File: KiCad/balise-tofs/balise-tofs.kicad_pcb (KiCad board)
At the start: 4 copper layers, 95.4 x 95.4 mm, 97 parts, among them J1 Vin, J10 Conn_02x05_Odd_Even, J11 Conn_02x05_Odd_Even, J12 Conn_02x05_Odd_Even, J13 Conn_02x05_Odd_Even, J14 Conn_02x05_Odd_Even, J15 Conn_02x05_Odd_Even, J16 Conn_02x05_Odd_Even, J17 Conn_02x05_Odd_Even, J18 Conn_02x05_Odd_Even, J19 Conn_02x05_Odd_Even, J2 Conn_01x03, J20 Conn_02x05_Odd_Even, J21 Conn_02x05_Odd_Even, Q1 Q_PMOS_GDS, U1 AP63203WU-7, U2 NUCLEO-G431KB, U3 PCA9535CPW, U4 AP63205WU-7, U5 74AHCT1G125

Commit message: ajout des plans
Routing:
- added copper zone on In2.Cu, net 3V3_SENS
- added copper zone on In1.Cu, net GND
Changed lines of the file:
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@@
 		(layer "Edge.Cuts")
+	)
+	(zone
+		(net 1)
+		(net_name "GND")
+		(layer "In1.Cu")
+		(hatch edge 0.5)
+		(connect_pads
+			(clearance 0.5)
+		)
+		(min_thickness 0.25)
+		(filled_areas_thickness no)
+		(fill yes
+			(thermal_gap 0.5)
+			(thermal_bridge_width 0.5)
+		)
+		(polygon
+			(pts
+				(xy 100.584 100.584) (xy 200.406 100.076) (xy 200.406 198.882) (xy 100.838 199.898)
+			)
+		)
+	)
+	(zone
+		(net 5)
+		(net_name "3V3_SENS")
+		(layer "In2.Cu")
+		(hatch edge 0.5)
+		(priority 1)
+		(connect_pads
+			(clearance 0.5)
+		)
+		(min_thickness 0.25)
+		(filled_areas_thickness no)
+		(fill yes
+			(thermal_gap 0.5)
+			(thermal_bridge_width 0.5)
+		)
+		(polygon
+			(pts
+				(xy 100.838 100.076) (xy 200.66 100.076) (xy 200.152 198.374) (xy 101.092 199.898)
+			)
+		)
 	)
 	(embedded_fonts no)

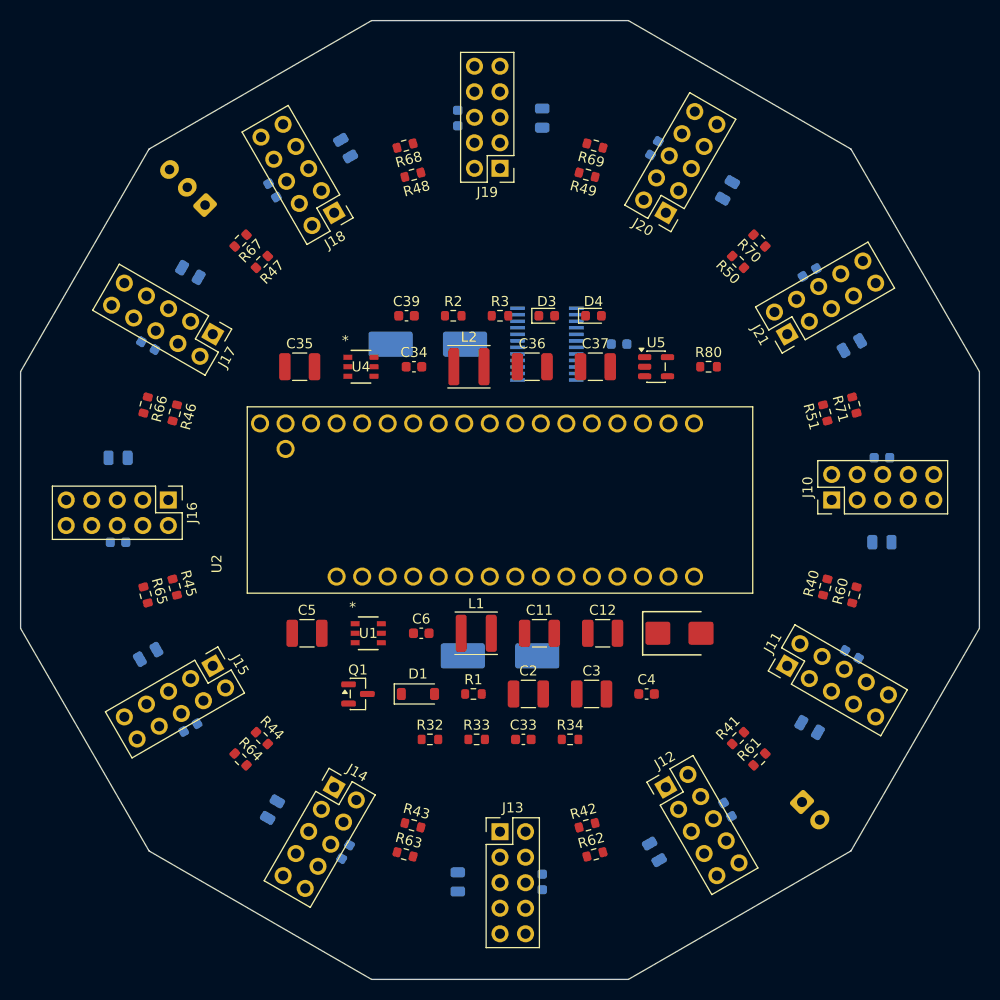
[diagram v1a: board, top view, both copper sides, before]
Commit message: passage à kicad 10 et début du routage
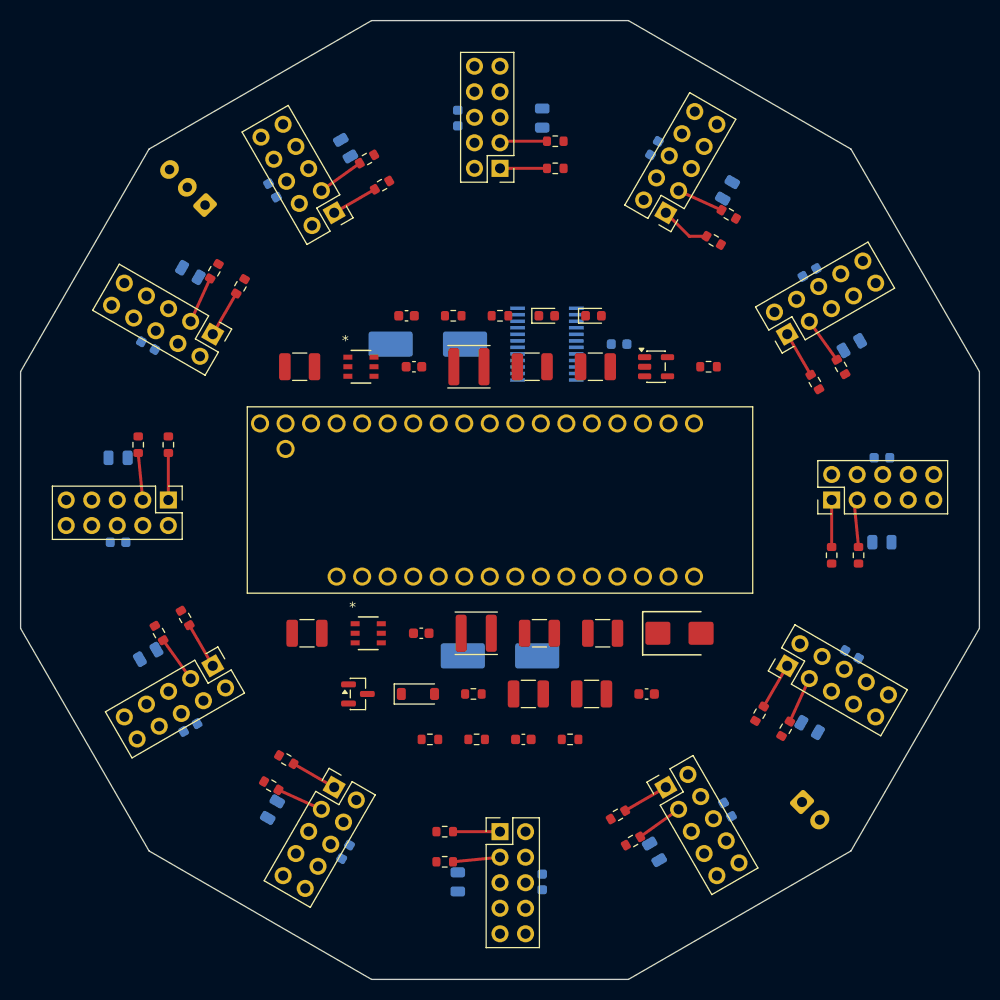
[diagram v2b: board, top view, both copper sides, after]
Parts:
- moved R45 4.83 mm to (116.1, 163.2), turned to -60 degrees
- moved R48 4.83 mm to (136.8, 116.1), turned to -150 degrees
- moved R42 4.83 mm to (163.2, 183.9), turned to 30 degrees
- moved R51 4.83 mm to (183.9, 136.8), turned to 120 degrees
- moved R44 4.83 mm to (127.2, 178.4), turned to -30 degrees
- moved R47 4.83 mm to (121.6, 127.2), turned to -120 degrees
- moved R41 4.83 mm to (178.4, 172.8), turned to 60 degrees
- moved R50 4.83 mm to (172.8, 121.6), turned to 150 degrees
- moved R46 4.83 mm to (114.0, 144.5), turned to -90 degrees
- moved R43 4.83 mm to (144.5, 186.0), turned to 0 degrees
- moved R49 4.61 mm to (155.5, 114.3), turned to 180 degrees
- moved R40 4.59 mm to (185.7, 155.5), turned to 90 degrees
- moved R62 4.55 mm to (161.7, 181.3), turned to 30 degrees
- moved R65 4.55 mm to (118.7, 161.7), turned to -60 degrees
- moved R68 4.55 mm to (138.3, 118.7), turned to -150 degrees
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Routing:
- net Net-(J20-Pin_1): track 0.00 -> 5.02 mm
- net Net-(J19-Pin_3): track 0.00 -> 4.74 mm
- net Net-(J20-Pin_3): track 0.00 -> 4.70 mm
- net Net-(J11-Pin_3): track 0.00 -> 4.70 mm
- net Net-(J17-Pin_3): track 0.00 -> 4.70 mm
- net Net-(J14-Pin_3): track 0.00 -> 4.70 mm
- net Net-(J13-Pin_3): track 0.00 -> 4.70 mm
- net Net-(J10-Pin_3): track 0.00 -> 4.70 mm
- net Net-(J16-Pin_3): track 0.00 -> 4.70 mm
- net Net-(J21-Pin_3): track 0.00 -> 4.70 mm
- net Net-(J18-Pin_3): track 0.00 -> 4.70 mm
- net Net-(J12-Pin_3): track 0.00 -> 4.70 mm
- net Net-(J15-Pin_3): track 0.00 -> 4.70 mm
- net Net-(J17-Pin_1): track 0.00 -> 4.68 mm
- net Net-(J14-Pin_1): track 0.00 -> 4.68 mm
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
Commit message: routage des trucs simples
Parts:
- moved J1 46.2 mm to (134.6, 171.7), turned to 0 degrees
- moved D2 35.8 mm to (132.1, 163.8), turned to 90 degrees
- moved R2 35.2 mm to (164.3, 161.3), turned to -90 degrees
- moved D4 34.5 mm to (140.0, 160.3)
- moved R34 34.4 mm to (154.9, 139.4), turned to 180 degrees
- moved D3 32.4 mm to (162.6, 163.1), turned to 90 degrees
- moved R3 29.4 mm to (143.3, 160.3), turned to 180 degrees
- moved C4 24.4 mm to (140.7, 164.3), turned to -90 degrees
- moved R80 23.3 mm to (149.9, 126.5), turned to -90 degrees
- moved U5 16.0 mm to (151.0, 130.0), turned to 180 degrees
- moved C37 14.8 mm to (146.3, 130.0), turned to 90 degrees
- moved C36 12.4 mm to (142.7, 130.0), turned to 90 degrees
- moved C48 9.96 mm to (135.4, 113.3)
- moved C40 9.95 mm to (189.0, 155.7)
- moved C50 9.93 mm to (174.5, 118.9)
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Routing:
- net VBAT: track 0.00 -> 83.6 mm, vias 0 -> 1
- net 5V: track 0.00 -> 45.8 mm, vias 0 -> 1
- net Net-(J2-Pin_2): track 0.00 -> 32.6 mm
- net GND: track 0.00 -> 29.4 mm, vias 0 -> 23
- net Net-(D1-A): track 0.00 -> 18.5 mm, vias 0 -> 2
- net 3V3_SENS: track 0.00 -> 7.01 mm, vias 0 -> 5
- net Net-(U1-SW): track 0.00 -> 6.48 mm
- net +BATT: track 0.00 -> 6.12 mm
- net Net-(U4-SW): track 0.00 -> 5.68 mm
- net VBAT_SENSE: track 0.00 -> 3.86 mm
- net SENS_OK: track 0.00 -> 2.96 mm
- net LED1: track 0.00 -> 2.89 mm
- net Net-(U4-BST): track 0.00 -> 2.85 mm
- net LED2: track 0.00 -> 2.73 mm
- net Net-(U1-BST): track 0.00 -> 2.47 mm
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
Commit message: finalisation du routage
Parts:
- added R20: 2.2k, Resistor_SMD:R_0603_1608Metric, F.Cu at (151.6, 145.6)
- added R21: 2.2k, Resistor_SMD:R_0603_1608Metric, F.Cu at (149.1, 145.6)
- added R22: 2.2k, Resistor_SMD:R_0603_1608Metric, F.Cu at (161.8, 153.6)
- added R23: 2.2k, Resistor_SMD:R_0603_1608Metric, F.Cu at (133.9, 154.2)
- J2: moved to F.Cu
- Q1: value Q_PMOS_GDS -> SI2307A
- R33: value 16k -> 15k
- moved C7 12.4 mm to (173.0, 129.3), turned to 90 degrees
- moved U3 8.16 mm to (167.9, 133.1), turned to 90 degrees
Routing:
- net SDA_B: track 0.00 -> 152.0 mm, vias 0 -> 5
- net SDA_A: track 0.00 -> 149.9 mm, vias 0 -> 1
- net SCL_A: track 0.00 -> 144.2 mm, vias 0 -> 3
- net INT_A: track 0.00 -> 142.5 mm, vias 0 -> 13
- net INT_B: track 0.00 -> 126.5 mm, vias 0 -> 13
- net GND: track 29.4 -> 150.7 mm, vias 23 -> 39
- net SCL_B: track 0.00 -> 118.5 mm, vias 0 -> 2
- net XSHUT4: track 0.00 -> 74.3 mm, vias 0 -> 1
- net 3V3_SENS: track 7.01 -> 79.9 mm, vias 5 -> 10
- net XSHUT5: track 0.00 -> 70.4 mm, vias 0 -> 1
- net XSHUT3: track 0.00 -> 67.9 mm, vias 0 -> 1
- net VBAT_SENSE: track 3.86 -> 62.0 mm
- net XSHUT6: track 0.00 -> 55.8 mm, vias 0 -> 1
- net XSHUT2: track 0.00 -> 53.6 mm, vias 0 -> 1
- net XSHUT7: track 0.00 -> 47.6 mm, vias 0 -> 1
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
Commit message: On replace des composant, on remet tout en top et on réduit la taille
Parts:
- C1, C20, C21, C22, C23, C24, C25, C26, C27, C28, C29, C30, C31, C38, C40, C41, C42, C43, C44, C45, C46, C47, C48, C49, C50, C51, C7, U3: moved to F.Cu
- moved J2 48.6 mm to (159.1, 147.1), turned to 0 degrees
- moved C38 32.9 mm to (172.0, 149.8), turned to 90 degrees
- moved C1 19.9 mm to (139.4, 149.1)
- moved C7 4.83 mm to (168.1, 129.3), turned to 0 degrees
- moved U3 2.96 mm to (165.2, 134.4), turned to 0 degrees
- moved C50 2.71 mm to (175.1, 116.2), turned to -60 degrees
- moved C41 2.17 mm to (183.1, 175.0), turned to -150 degrees
- moved R46 2.02 mm to (114.3, 146.5)
- moved C47 1.98 mm to (116.5, 126.7), turned to -120 degrees
- moved C44 1.62 mm to (125.4, 182.8), turned to 120 degrees
- moved C51 1.49 mm to (188.3, 134.3), turned to -120 degrees
- moved C42 1.37 mm to (165.4, 187.7), turned to 150 degrees
- moved C45 1.28 mm to (112.3, 165.2), turned to 60 degrees
- moved C48 1.27 mm to (134.6, 112.3), turned to -30 degrees
- moved C27 0.95 mm to (118.1, 127.3), turned to -120 degrees
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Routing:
- net 5V: track 45.8 -> 106.5 mm, vias 1 -> 5
- net VBAT: track 83.6 -> 96.0 mm, vias 1 -> 2
- net GND: track 150.7 -> 162.1 mm
- net XSHUT0: track 33.5 -> 44.4 mm, vias 1 -> 2
- net XSHUT8: track 34.9 -> 44.8 mm, vias 1 -> 2
- net XSHUT9: track 20.0 -> 29.5 mm, vias 1 -> 2
- net 3V3_SENS: track 79.9 -> 88.5 mm
- net XSHUT1: track 43.3 -> 51.8 mm, vias 1 -> 2
- net XSHUT10: track 11.9 -> 19.9 mm, vias 1 -> 2
- net XSHUT2: track 53.6 -> 59.2 mm, vias 1 -> 2
- net Net-(J2-Pin_2): track 32.6 -> 28.3 mm, vias 0 -> 2
- net XSHUT5: track 70.4 -> 66.6 mm, vias 1 -> 2
- net XSHUT3: track 67.9 -> 71.4 mm, vias 1 -> 2
- net XSHUT11: track 22.9 -> 19.5 mm, vias 1 -> 2
- net INT_B: track 126.5 -> 129.3 mm
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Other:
- board size 95.4 x 95.4 mm -> 91.4 x 91.4 mm

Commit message: On fini de tout bien router
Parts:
- U2: moved to B.Cu
- moved R22 28.2 mm to (133.6, 154.5)
- moved R2 28.0 mm to (136.3, 160.5), turned to 0 degrees
- moved R23 27.7 mm to (161.5, 154.5)
- moved D3 23.3 mm to (139.4, 160.5), turned to 180 degrees
- moved D4 16.2 mm to (155.3, 154.9), turned to 180 degrees
- moved R34 13.8 mm to (142.0, 144.3)
- moved R3 10.2 mm to (152.0, 154.9), turned to 0 degrees
- moved R20 6.61 mm to (145.0, 145.4)
- moved U2 4.71 mm to (145.3, 149.9)
- moved R21 2.30 mm to (146.8, 145.4)
- moved J2 2.11 mm to (157.0, 147.1)
- moved C1 1.02 mm to (139.4, 150.1)
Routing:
- net SDA_B: track 152.0 -> 121.7 mm, vias 5 -> 2
- net SCL_B: track 118.5 -> 144.1 mm
- net VBAT_SENSE: track 62.0 -> 37.2 mm, vias 0 -> 1
- net VBAT: track 96.0 -> 91.3 mm, vias 2 -> 0
- net INT_B: track 129.3 -> 125.3 mm
- net SDA_A: track 151.7 -> 155.2 mm, vias 3 -> 2
- net LED_DATA: track 35.0 -> 38.4 mm, vias 1 -> 2
- net LED1: track 2.89 -> 5.71 mm
- net GND: track 162.1 -> 164.6 mm
- net INT_A: track 142.5 -> 140.3 mm, vias 13 -> 10
- net 5V: track 106.5 -> 108.6 mm
- net SCL_A: track 143.2 -> 145.0 mm
- net SENS_OK: track 2.96 -> 2.03 mm
- net 3V3_SENS: track 88.5 -> 89.2 mm
- net XSHUT4: track 77.0 -> 77.6 mm
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
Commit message: dernières mise à jour avant production
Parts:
- added D5: D_Schottky, Diode_SMD:D_SOD-123, F.Cu at (161.5, 149.5)
- added J22: Cavalier, Connector_JST:JST_XH_B2B-XH-A_1x02_P2.50mm_Vertical, F.Cu at (156.2, 149.8)
- L1: value 3.3uH -> 3.9uH
- moved J2 20.8 mm to (176.5, 154.1), turned to 90 degrees
- moved C38 5.79 mm to (167.4, 153.3)
- turned D2 to -90 degrees
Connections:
- D2 pad 1: GND -> VBAT
- D2 pad 2: VBAT -> GND
- U2 pad CN3_4: unconnected-(U2-5V-PadCN3_4) -> Net-(J22-Pin_2)
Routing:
- net Net-(J2-Pin_2): track 28.1 -> 44.9 mm, vias 1 -> 2
- net Net-(J22-Pin_2): track 0.00 -> 6.04 mm
- net Net-(D5-K): track 0.00 -> 5.77 mm
- net 5V: track 108.6 -> 110.4 mm, vias 5 -> 3
- net GND: track 164.6 -> 163.1 mm
- net XSHUT2: vias 2 -> 4
